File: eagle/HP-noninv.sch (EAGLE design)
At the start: 20 parts, among them IC1 OPA2134, IC2 TLE2426CLP

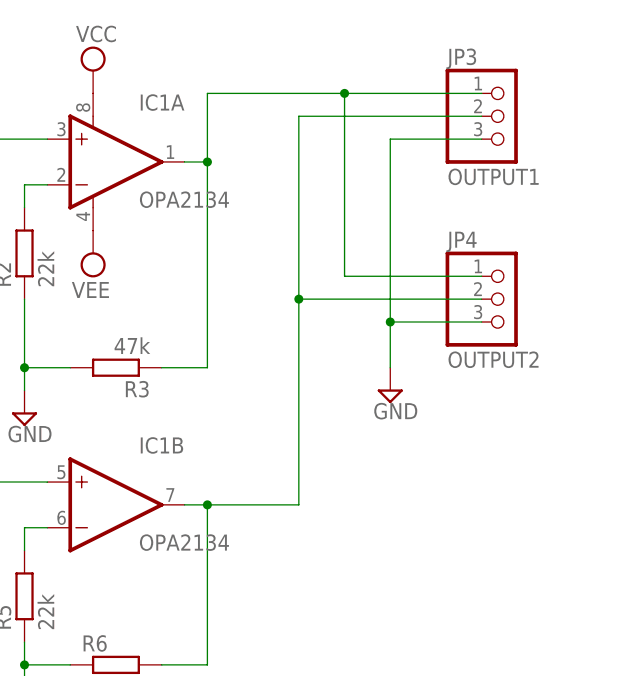
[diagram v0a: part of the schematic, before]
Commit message: 保護抵抗追加
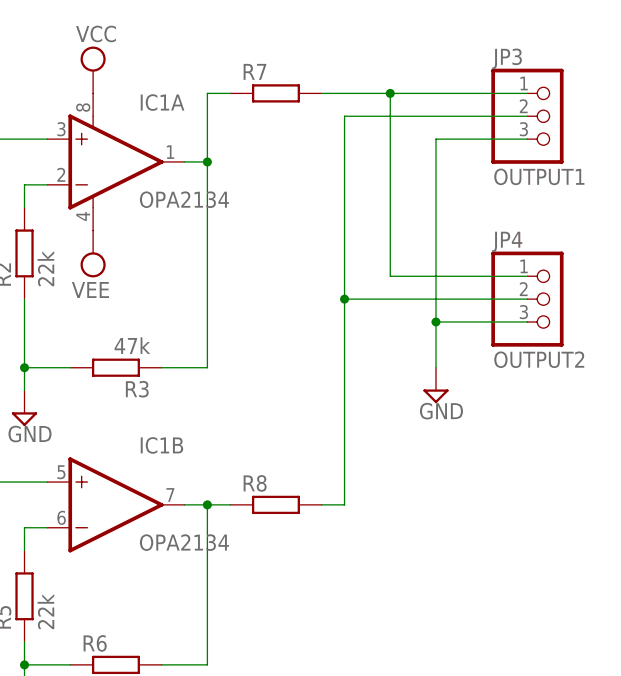
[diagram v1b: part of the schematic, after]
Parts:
- added R7, R8: (no value), rcl:R-EU_0207/7
- R6: device rcl:R-EU_0207/2V -> rcl:R-EU_0207/7
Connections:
- new net N$2: IC1A.OUT, R3.1, R7.1
- new net N$4: IC1B.OUT, R6.2, R8.1
- net N$11: now also R8.2; no longer IC1B.OUT, R6.2
- net N$8: now also R7.2; no longer IC1A.OUT, R3.1
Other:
- moved on the sheet: JP3, JP4
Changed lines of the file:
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@@
 <part name="SUPPLY9" library="supply2" deviceset="GND" device=""/>
 <part name="R5" library="rcl" deviceset="R-EU_" device="0207/7" value="22k"/>
-<part name="R6" library="rcl" deviceset="R-EU_" device="0207/2V" value="47k"/>
+<part name="R6" library="rcl" deviceset="R-EU_" device="0207/7" value="47k"/>
 <part name="SUPPLY10" library="supply2" deviceset="GND" device=""/>
 <part name="JP1" library="pinhead" deviceset="PINHD-1X2" device="" value="PWR"/>
@@
 <part name="JP3" library="pinhead" deviceset="PINHD-1X3" device="" value="OUTPUT1"/>
 <part name="JP4" library="pinhead" deviceset="PINHD-1X3" device="" value="OUTPUT2"/>
+<part name="R7" library="rcl" deviceset="R-EU_" device="0207/7"/>
+<part name="R8" library="rcl" deviceset="R-EU_" device="0207/7"/>
 </parts>
 <sheets>
@@
 <instance part="SUPPLY7" gate="G$1" x="99.06" y="162.56"/>
 <instance part="SUPPLY8" gate="G$1" x="99.06" y="142.24" rot="R180"/>
-<instance part="SUPPLY9" gate="GND" x="132.08" y="127"/>
+<instance part="SUPPLY9" gate="GND" x="137.16" y="127"/>
 <instance part="R5" gate="G$1" x="91.44" y="104.14" rot="R90"/>
 <instance part="R6" gate="G$1" x="101.6" y="96.52"/>
@@
 <instance part="SUPPLY17" gate="GND" x="116.84" y="48.26"/>
 <instance part="JP2" gate="A" x="43.18" y="152.4" rot="MR0"/>
-<instance part="JP3" gate="A" x="144.78" y="157.48"/>
-<instance part="JP4" gate="A" x="144.78" y="137.16"/>
+<instance part="JP3" gate="A" x="149.86" y="157.48"/>
+<instance part="JP4" gate="A" x="149.86" y="137.16"/>
+<instance part="R7" gate="G$1" x="119.38" y="160.02"/>
+<instance part="R8" gate="G$1" x="119.38" y="114.3"/>
 </instances>
 <busses>
@@
 <pinref part="JP4" gate="A" pin="3"/>
 <pinref part="SUPPLY9" gate="GND" pin="GND"/>
-<wire x1="142.24" y1="134.62" x2="132.08" y2="134.62" width="0.1524" layer="91"/>
-<wire x1="132.08" y1="134.62" x2="132.08" y2="129.54" width="0.1524" layer="91"/>
+<wire x1="147.32" y1="134.62" x2="137.16" y2="134.62" width="0.1524" layer="91"/>
+<wire x1="137.16" y1="134.62" x2="137.16" y2="129.54" width="0.1524" layer="91"/>
 <pinref part="JP3" gate="A" pin="3"/>
-<wire x1="142.24" y1="154.94" x2="132.08" y2="154.94" width="0.1524" layer="91"/>
-<wire x1="132.08" y1="154.94" x2="132.08" y2="134.62" width="0.1524" layer="91"/>
-<junction x="132.08" y="134.62"/>
+<wire x1="147.32" y1="154.94" x2="137.16" y2="154.94" width="0.1524" layer="91"/>
+<wire x1="137.16" y1="154.94" x2="137.16" y2="134.62" width="0.1524" layer="91"/>
+<junction x="137.16" y="134.62"/>
 </segment>
 <segment>
@@
 <net name="N$8" class="0">
 <segment>
-<pinref part="IC1" gate="A" pin="OUT"/>
-<wire x1="109.22" y1="152.4" x2="111.76" y2="152.4" width="0.1524" layer="91"/>
-<wire x1="111.76" y1="152.4" x2="111.76" y2="129.54" width="0.1524" layer="91"/>
-<pinref part="R3" gate="G$1" pin="1"/>
-<wire x1="111.76" y1="129.54" x2="106.68" y2="129.54" width="0.1524" layer="91"/>
 <pinref part="JP3" gate="A" pin="1"/>
-<wire x1="142.24" y1="160.02" x2="127" y2="160.02" width="0.1524" layer="91"/>
-<wire x1="127" y1="160.02" x2="111.76" y2="160.02" width="0.1524" layer="91"/>
-<wire x1="111.76" y1="160.02" x2="111.76" y2="152.4" width="0.1524" layer="91"/>
-<junction x="111.76" y="152.4"/>
+<wire x1="147.32" y1="160.02" x2="132.08" y2="160.02" width="0.1524" layer="91"/>
 <pinref part="JP4" gate="A" pin="1"/>
-<wire x1="142.24" y1="139.7" x2="127" y2="139.7" width="0.1524" layer="91"/>
-<wire x1="127" y1="139.7" x2="127" y2="160.02" width="0.1524" layer="91"/>
-<junction x="127" y="160.02"/>
+<wire x1="147.32" y1="139.7" x2="132.08" y2="139.7" width="0.1524" layer="91"/>
+<wire x1="132.08" y1="139.7" x2="132.08" y2="160.02" width="0.1524" layer="91"/>
+<pinref part="R7" gate="G$1" pin="2"/>
+<wire x1="124.46" y1="160.02" x2="132.08" y2="160.02" width="0.1524" layer="91"/>
+<junction x="132.08" y="160.02"/>
 </segment>
 </net>
@@
 <net name="N$11" class="0">
 <segment>
-<pinref part="IC1" gate="B" pin="OUT"/>
-<wire x1="109.22" y1="114.3" x2="111.76" y2="114.3" width="0.1524" layer="91"/>
-<wire x1="111.76" y1="114.3" x2="111.76" y2="96.52" width="0.1524" layer="91"/>
-<wire x1="121.92" y1="157.48" x2="121.92" y2="137.16" width="0.1524" layer="91"/>
-<wire x1="121.92" y1="137.16" x2="121.92" y2="114.3" width="0.1524" layer="91"/>
-<wire x1="121.92" y1="114.3" x2="111.76" y2="114.3" width="0.1524" layer="91"/>
-<junction x="111.76" y="114.3"/>
+<wire x1="127" y1="157.48" x2="127" y2="137.16" width="0.1524" layer="91"/>
+<wire x1="127" y1="137.16" x2="127" y2="114.3" width="0.1524" layer="91"/>
 <pinref part="JP3" gate="A" pin="2"/>
-<wire x1="121.92" y1="157.48" x2="142.24" y2="157.48" width="0.1524" layer="91"/>
+<wire x1="127" y1="157.48" x2="147.32" y2="157.48" width="0.1524" layer="91"/>
 <pinref part="JP4" gate="A" pin="2"/>
-<wire x1="142.24" y1="137.16" x2="121.92" y2="137.16" width="0.1524" layer="91"/>
-<junction x="121.92" y="137.16"/>
-<pinref part="R6" gate="G$1" pin="2"/>
-<wire x1="106.68" y1="96.52" x2="111.76" y2="96.52" width="0.1524" layer="91"/>
+<wire x1="147.32" y1="137.16" x2="127" y2="137.16" width="0.1524" layer="91"/>
+<junction x="127" y="137.16"/>
+<pinref part="R8" gate="G$1" pin="2"/>
+<wire x1="124.46" y1="114.3" x2="127" y2="114.3" width="0.1524" layer="91"/>
 </segment>
 </net>
@@
 </segment>
 </net>
+<net name="N$2" class="0">
+<segment>
+<pinref part="R3" gate="G$1" pin="1"/>
+<wire x1="111.76" y1="129.54" x2="106.68" y2="129.54" width="0.1524" layer="91"/>
+<wire x1="111.76" y1="152.4" x2="111.76" y2="129.54" width="0.1524" layer="91"/>
+<wire x1="111.76" y1="160.02" x2="111.76" y2="152.4" width="0.1524" layer="91"/>
+<junction x="111.76" y="152.4"/>
+<pinref part="IC1" gate="A" pin="OUT"/>
+<wire x1="109.22" y1="152.4" x2="111.76" y2="152.4" width="0.1524" layer="91"/>
+<pinref part="R7" gate="G$1" pin="1"/>
+<wire x1="111.76" y1="160.02" x2="114.3" y2="160.02" width="0.1524" layer="91"/>
+</segment>
+</net>
+<net name="N$4" class="0">
+<segment>
+<pinref part="IC1" gate="B" pin="OUT"/>
+<wire x1="109.22" y1="114.3" x2="111.76" y2="114.3" width="0.1524" layer="91"/>
+<wire x1="111.76" y1="114.3" x2="111.76" y2="96.52" width="0.1524" layer="91"/>
+<pinref part="R6" gate="G$1" pin="2"/>
+<wire x1="106.68" y1="96.52" x2="111.76" y2="96.52" width="0.1524" layer="91"/>
+<pinref part="R8" gate="G$1" pin="1"/>
+<wire x1="114.3" y1="114.3" x2="111.76" y2="114.3" width="0.1524" layer="91"/>
+<junction x="111.76" y="114.3"/>
+</segment>
+</net>

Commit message: ケミコンを倒して配置
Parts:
- C3, C4: device rcl:CPOL-EUE5-6 -> rcl:CPOL-EUTT5D6L
- R11: value 1k -> 4.7k
- R7, R8: value (none) -> 22
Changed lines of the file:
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@@
 <part name="SUPPLY10" library="supply2" deviceset="GND" device=""/>
 <part name="JP1" library="pinhead" deviceset="PINHD-1X2" device="" value="PWR"/>
-<part name="R11" library="rcl" deviceset="R-EU_" device="0207/7" value="1k"/>
+<part name="R11" library="rcl" deviceset="R-EU_" device="0207/7" value="4.7k"/>
 <part name="LED1" library="led" deviceset="LED" device="3MM" value="Blue"/>
 <part name="IC2" library="tle2426" deviceset="TLE2426*L" device="P" technology="C"/>
-<part name="C3" library="rcl" deviceset="CPOL-EU" device="E5-6" value="100u"/>
-<part name="C4" library="rcl" deviceset="CPOL-EU" device="E5-6" value="100u"/>
+<part name="C3" library="rcl" deviceset="CPOL-EU" device="TT5D6L" value="100u"/>
+<part name="C4" library="rcl" deviceset="CPOL-EU" device="TT5D6L" value="100u"/>
 <part name="C5" library="rcl" deviceset="C-EU" device="050-024X044" value="0.1u"/>
 <part name="C6" library="rcl" deviceset="C-EU" device="050-024X044" value="0.1u"/>
@@
 <part name="JP3" library="pinhead" deviceset="PINHD-1X3" device="" value="OUTPUT1"/>
 <part name="JP4" library="pinhead" deviceset="PINHD-1X3" device="" value="OUTPUT2"/>
-<part name="R7" library="rcl" deviceset="R-EU_" device="0207/7"/>
-<part name="R8" library="rcl" deviceset="R-EU_" device="0207/7"/>
+<part name="R7" library="rcl" deviceset="R-EU_" device="0207/7" value="22"/>
+<part name="R8" library="rcl" deviceset="R-EU_" device="0207/7" value="22"/>
 </parts>
 <sheets>

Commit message: 積セラの配置を変更
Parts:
- C5: device rcl:C-EU050-024X044 -> rcl:C-EU025-024X044
- R2, R5: value 22k -> 12k
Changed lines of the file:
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@@
 <part name="SUPPLY5" library="supply2" deviceset="GND" device=""/>
 <part name="IC1" library="burr-brown" deviceset="OPA2134" device="P" value="OPA2134"/>
-<part name="R2" library="rcl" deviceset="R-EU_" device="0207/7" value="22k"/>
+<part name="R2" library="rcl" deviceset="R-EU_" device="0207/7" value="12k"/>
 <part name="R3" library="rcl" deviceset="R-EU_" device="0207/7" value="47k"/>
 <part name="SUPPLY6" library="supply2" deviceset="GND" device=""/>
@@
 <part name="SUPPLY8" library="supply2" deviceset="VEE" device=""/>
 <part name="SUPPLY9" library="supply2" deviceset="GND" device=""/>
-<part name="R5" library="rcl" deviceset="R-EU_" device="0207/7" value="22k"/>
+<part name="R5" library="rcl" deviceset="R-EU_" device="0207/7" value="12k"/>
 <part name="R6" library="rcl" deviceset="R-EU_" device="0207/7" value="47k"/>
 <part name="SUPPLY10" library="supply2" deviceset="GND" device=""/>
@@
 <part name="C3" library="rcl" deviceset="CPOL-EU" device="TT5D6L" value="100u"/>
 <part name="C4" library="rcl" deviceset="CPOL-EU" device="TT5D6L" value="100u"/>
-<part name="C5" library="rcl" deviceset="C-EU" device="050-024X044" value="0.1u"/>
+<part name="C5" library="rcl" deviceset="C-EU" device="025-024X044" value="0.1u"/>
 <part name="C6" library="rcl" deviceset="C-EU" device="050-024X044" value="0.1u"/>
 <part name="SUPPLY21" library="supply2" deviceset="VEE" device=""/>

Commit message: Hardware完成
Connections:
- net GND: now also R2.2; no longer R2.1, R3.2, R6.1
- net N$7: now also R2.1, R3.2; no longer R2.2
- net N$9: now also R6.1
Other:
- moved on the sheet: R2, R5, R6
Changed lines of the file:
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@@
 <instance part="IC1" gate="A" x="101.6" y="152.4"/>
 <instance part="IC1" gate="B" x="101.6" y="114.3"/>
-<instance part="R2" gate="G$1" x="91.44" y="142.24" rot="R90"/>
+<instance part="R2" gate="G$1" x="83.82" y="129.54" rot="R180"/>
 <instance part="R3" gate="G$1" x="101.6" y="129.54" rot="R180"/>
-<instance part="SUPPLY6" gate="GND" x="91.44" y="124.46"/>
+<instance part="SUPPLY6" gate="GND" x="76.2" y="124.46"/>
 <instance part="SUPPLY7" gate="G$1" x="99.06" y="162.56"/>
 <instance part="SUPPLY8" gate="G$1" x="99.06" y="142.24" rot="R180"/>
 <instance part="SUPPLY9" gate="GND" x="137.16" y="127"/>
-<instance part="R5" gate="G$1" x="91.44" y="104.14" rot="R90"/>
-<instance part="R6" gate="G$1" x="101.6" y="96.52"/>
-<instance part="SUPPLY10" gate="GND" x="91.44" y="91.44"/>
+<instance part="R5" gate="G$1" x="83.82" y="91.44"/>
+<instance part="R6" gate="G$1" x="101.6" y="91.44"/>
+<instance part="SUPPLY10" gate="GND" x="76.2" y="86.36"/>
 <instance part="JP1" gate="G$1" x="43.18" y="66.04" rot="MR0"/>
 <instance part="R11" gate="G$1" x="66.04" y="60.96" rot="R90"/>
@@
 </segment>
 <segment>
-<pinref part="R3" gate="G$1" pin="2"/>
-<wire x1="96.52" y1="129.54" x2="91.44" y2="129.54" width="0.1524" layer="91"/>
-<pinref part="R2" gate="G$1" pin="1"/>
-<wire x1="91.44" y1="129.54" x2="91.44" y2="137.16" width="0.1524" layer="91"/>
-<pinref part="SUPPLY6" gate="GND" pin="GND"/>
-<wire x1="91.44" y1="127" x2="91.44" y2="129.54" width="0.1524" layer="91"/>
-<junction x="91.44" y="129.54"/>
-</segment>
-<segment>
 <pinref part="SUPPLY5" gate="GND" pin="GND"/>
 <pinref part="R4" gate="G$1" pin="1"/>
 <wire x1="76.2" y1="101.6" x2="76.2" y2="104.14" width="0.1524" layer="91"/>
-</segment>
-<segment>
-<pinref part="R5" gate="G$1" pin="1"/>
-<wire x1="91.44" y1="99.06" x2="91.44" y2="96.52" width="0.1524" layer="91"/>
-<pinref part="SUPPLY10" gate="GND" pin="GND"/>
-<pinref part="R6" gate="G$1" pin="1"/>
-<wire x1="91.44" y1="96.52" x2="91.44" y2="93.98" width="0.1524" layer="91"/>
-<wire x1="96.52" y1="96.52" x2="91.44" y2="96.52" width="0.1524" layer="91"/>
-<junction x="91.44" y="96.52"/>
 </segment>
 <segment>
@@
 <wire x1="53.34" y1="152.4" x2="53.34" y2="144.78" width="0.1524" layer="91"/>
 </segment>
+<segment>
+<pinref part="R2" gate="G$1" pin="2"/>
+<pinref part="SUPPLY6" gate="GND" pin="GND"/>
+<wire x1="78.74" y1="129.54" x2="76.2" y2="129.54" width="0.1524" layer="91"/>
+<wire x1="76.2" y1="129.54" x2="76.2" y2="127" width="0.1524" layer="91"/>
+</segment>
+<segment>
+<pinref part="SUPPLY10" gate="GND" pin="GND"/>
+<wire x1="76.2" y1="91.44" x2="76.2" y2="88.9" width="0.1524" layer="91"/>
+<pinref part="R5" gate="G$1" pin="1"/>
+<wire x1="76.2" y1="91.44" x2="78.74" y2="91.44" width="0.1524" layer="91"/>
+</segment>
 </net>
 <net name="N$5" class="0">
@@
 <net name="N$7" class="0">
 <segment>
-<pinref part="R2" gate="G$1" pin="2"/>
-<wire x1="91.44" y1="147.32" x2="91.44" y2="149.86" width="0.1524" layer="91"/>
 <pinref part="IC1" gate="A" pin="-IN"/>
 <wire x1="91.44" y1="149.86" x2="93.98" y2="149.86" width="0.1524" layer="91"/>
+<pinref part="R2" gate="G$1" pin="1"/>
+<pinref part="R3" gate="G$1" pin="2"/>
+<wire x1="88.9" y1="129.54" x2="91.44" y2="129.54" width="0.1524" layer="91"/>
+<wire x1="91.44" y1="129.54" x2="96.52" y2="129.54" width="0.1524" layer="91"/>
+<wire x1="91.44" y1="149.86" x2="91.44" y2="129.54" width="0.1524" layer="91"/>
+<junction x="91.44" y="129.54"/>
 </segment>
 </net>
@@
 <net name="N$9" class="0">
 <segment>
-<pinref part="R5" gate="G$1" pin="2"/>
-<wire x1="91.44" y1="109.22" x2="91.44" y2="111.76" width="0.1524" layer="91"/>
 <pinref part="IC1" gate="B" pin="-IN"/>
 <wire x1="91.44" y1="111.76" x2="93.98" y2="111.76" width="0.1524" layer="91"/>
+<pinref part="R6" gate="G$1" pin="1"/>
+<wire x1="91.44" y1="91.44" x2="96.52" y2="91.44" width="0.1524" layer="91"/>
+<wire x1="91.44" y1="111.76" x2="91.44" y2="91.44" width="0.1524" layer="91"/>
+<pinref part="R5" gate="G$1" pin="2"/>
+<wire x1="88.9" y1="91.44" x2="91.44" y2="91.44" width="0.1524" layer="91"/>
+<junction x="91.44" y="91.44"/>
 </segment>
 </net>
@@
 <segment>
 <pinref part="IC1" gate="B" pin="OUT"/>
-<wire x1="109.22" y1="114.3" x2="111.76" y2="114.3" width="0.1524" layer="91"/>
-<wire x1="111.76" y1="114.3" x2="111.76" y2="96.52" width="0.1524" layer="91"/>
-<pinref part="R6" gate="G$1" pin="2"/>
-<wire x1="106.68" y1="96.52" x2="111.76" y2="96.52" width="0.1524" layer="91"/>
 <pinref part="R8" gate="G$1" pin="1"/>
 <wire x1="114.3" y1="114.3" x2="111.76" y2="114.3" width="0.1524" layer="91"/>
+<pinref part="R6" gate="G$1" pin="2"/>
+<wire x1="111.76" y1="114.3" x2="109.22" y2="114.3" width="0.1524" layer="91"/>
+<wire x1="106.68" y1="91.44" x2="111.76" y2="91.44" width="0.1524" layer="91"/>
+<wire x1="111.76" y1="91.44" x2="111.76" y2="114.3" width="0.1524" layer="91"/>
 <junction x="111.76" y="114.3"/>
 </segment>
